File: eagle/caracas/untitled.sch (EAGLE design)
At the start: 26 parts, among them IC1 4027N, Q1 IRFP250, X1 22-23-2021, X2 22-23-2021, X3 22-23-2041, X4 22-23-2041, X5 22-23-2021, X6 22-23-2021

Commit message: Schematic and board finished (at least R1)
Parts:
- Q1: value IRFP250 -> IRLZ44Z; device transistor-power:IRFP250 -> transistor-power:IRLZ44Z
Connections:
- net +12V_IGN: now also U$2G$4.P$1; no longer U$2G$3.P$1
- net +3.3V: now also X4-1.S, X4-2.S; no longer X3-1.S, X4-4.S
- net ANA_1: now also X4-4.S; no longer X4-2.S
- net GND: no longer X4-1.S
- net VCC: now also U$2G$3.P$1; no longer U$2G$2.P$1
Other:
- moved on the sheet: X3-1, X4-1, X4-2, X4-4
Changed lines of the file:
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@@
 <grid distance="0.1" unitdist="inch" unit="inch" style="lines" multiple="1" display="no" altdistance="0.01" altunitdist="inch" altunit="inch"/>
 <layers>
-<layer number="1" name="Top" color="4" fill="1" visible="no" active="no"/>
-<layer number="16" name="Bottom" color="1" fill="1" visible="no" active="no"/>
-<layer number="17" name="Pads" color="2" fill="1" visible="no" active="no"/>
-<layer number="18" name="Vias" color="2" fill="1" visible="no" active="no"/>
-<layer number="19" name="Unrouted" color="6" fill="1" visible="no" active="no"/>
-<layer number="20" name="Dimension" color="15" fill="1" visible="no" active="no"/>
-<layer number="21" name="tPlace" color="7" fill="1" visible="no" active="no"/>
-<layer number="22" name="bPlace" color="7" fill="1" visible="no" active="no"/>
-<layer number="23" name="tOrigins" color="15" fill="1" visible="no" active="no"/>
-<layer number="24" name="bOrigins" color="15" fill="1" visible="no" active="no"/>
-<layer number="25" name="tNames" color="7" fill="1" visible="no" active="no"/>
-<layer number="26" name="bNames" color="7" fill="1" visible="no" active="no"/>
-<layer number="27" name="tValues" color="7" fill="1" visible="no" active="no"/>
-<layer number="28" name="bValues" color="7" fill="1" visible="no" active="no"/>
+<layer number="1" name="Top" color="4" fill="1" visible="yes" active="no"/>
+<layer number="16" name="Bottom" color="1" fill="1" visible="yes" active="no"/>
+<layer number="17" name="Pads" color="2" fill="1" visible="yes" active="no"/>
+<layer number="18" name="Vias" color="2" fill="1" visible="yes" active="no"/>
+<layer number="19" name="Unrouted" color="6" fill="1" visible="yes" active="no"/>
+<layer number="20" name="Dimension" color="15" fill="1" visible="yes" active="no"/>
+<layer number="21" name="tPlace" color="7" fill="1" visible="yes" active="no"/>
+<layer number="22" name="bPlace" color="7" fill="1" visible="yes" active="no"/>
+<layer number="23" name="tOrigins" color="15" fill="1" visible="yes" active="no"/>
+<layer number="24" name="bOrigins" color="15" fill="1" visible="yes" active="no"/>
+<layer number="25" name="tNames" color="7" fill="1" visible="yes" active="no"/>
+<layer number="26" name="bNames" color="7" fill="1" visible="yes" active="no"/>
+<layer number="27" name="tValues" color="7" fill="1" visible="yes" active="no"/>
+<layer number="28" name="bValues" color="7" fill="1" visible="yes" active="no"/>
 <layer number="29" name="tStop" color="7" fill="3" visible="no" active="no"/>
 <layer number="30" name="bStop" color="7" fill="6" visible="no" active="no"/>
@@
 <layer number="35" name="tGlue" color="7" fill="4" visible="no" active="no"/>
 <layer number="36" name="bGlue" color="7" fill="5" visible="no" active="no"/>
-<layer number="37" name="tTest" color="7" fill="1" visible="no" active="no"/>
-<layer number="38" name="bTest" color="7" fill="1" visible="no" active="no"/>
+<layer number="37" name="tTest" color="7" fill="1" visible="yes" active="no"/>
+<layer number="38" name="bTest" color="7" fill="1" visible="yes" active="no"/>
 <layer number="39" name="tKeepout" color="4" fill="11" visible="no" active="no"/>
 <layer number="40" name="bKeepout" color="1" fill="11" visible="no" active="no"/>
@@
 <layer number="44" name="Drills" color="7" fill="1" visible="no" active="no"/>
 <layer number="45" name="Holes" color="7" fill="1" visible="no" active="no"/>
-<layer number="46" name="Milling" color="3" fill="1" visible="no" active="no"/>
-<layer number="47" name="Measures" color="7" fill="1" visible="no" active="no"/>
-<layer number="48" name="Document" color="7" fill="1" visible="no" active="no"/>
-<layer number="49" name="Reference" color="7" fill="1" visible="no" active="no"/>
-<layer number="51" name="tDocu" color="7" fill="1" visible="no" active="no"/>
-<layer number="52" name="bDocu" color="7" fill="1" visible="no" active="no"/>
+<layer number="46" name="Milling" color="3" fill="1" visible="yes" active="no"/>
+<layer number="47" name="Measures" color="7" fill="1" visible="yes" active="no"/>
+<layer number="48" name="Document" color="7" fill="1" visible="yes" active="no"/>
+<layer number="49" name="Reference" color="7" fill="1" visible="yes" active="no"/>
+<layer number="51" name="tDocu" color="7" fill="1" visible="yes" active="no"/>
+<layer number="52" name="bDocu" color="7" fill="1" visible="yes" active="no"/>
 <layer number="91" name="Nets" color="2" fill="1" visible="yes" active="yes"/>
 <layer number="92" name="Busses" color="1" fill="1" visible="yes" active="yes"/>
@@
 <part name="R5" library="rcl" deviceset="R-EU_" device="0207/10"/>
 <part name="R3" library="rcl" deviceset="R-EU_" device="0207/10"/>
-<part name="Q1" library="transistor-power" deviceset="IRFP25*" device="" technology="0"/>
 <part name="SUPPLY3" library="supply2" deviceset="GND" device=""/>
 <part name="R8" library="rcl" deviceset="R-EU_" device="0207/10"/>
@@
 <part name="X3" library="con-molex" deviceset="22-23-2041" device=""/>
 <part name="X4" library="con-molex" deviceset="22-23-2041" device=""/>
+<part name="Q1" library="transistor-power" deviceset="IRLZ44Z" device=""/>
 </parts>
 <sheets>
@@
 <instance part="R5" gate="G$1" x="43.18" y="38.1" rot="R270"/>
 <instance part="R3" gate="G$1" x="99.06" y="45.72"/>
-<instance part="Q1" gate="G$1" x="114.3" y="48.26"/>
 <instance part="SUPPLY3" gate="GND" x="-48.26" y="2.54"/>
 <instance part="R8" gate="G$1" x="-76.2" y="-12.7" rot="R90"/>
@@
 <instance part="R11" gate="G$1" x="88.9" y="-43.18" rot="R90"/>
 <instance part="R12" gate="G$1" x="93.98" y="-43.18" rot="R90"/>
-<instance part="X3" gate="-1" x="-63.5" y="-38.1" rot="R270"/>
+<instance part="X4" gate="-1" x="-63.5" y="-38.1" rot="R270"/>
 <instance part="X3" gate="-2" x="-66.04" y="-38.1" rot="R270"/>
 <instance part="X3" gate="-3" x="-68.58" y="-38.1" rot="R270"/>
 <instance part="X3" gate="-4" x="-71.12" y="-38.1" rot="R270"/>
-<instance part="X4" gate="-1" x="-53.34" y="-38.1" rot="R270"/>
-<instance part="X4" gate="-2" x="-55.88" y="-38.1" rot="R270"/>
+<instance part="X3" gate="-1" x="-53.34" y="-38.1" rot="R270"/>
+<instance part="X4" gate="-4" x="-55.88" y="-38.1" rot="R270"/>
 <instance part="X4" gate="-3" x="-58.42" y="-38.1" rot="R270"/>
-<instance part="X4" gate="-4" x="-60.96" y="-38.1" rot="R270"/>
-<instance part="U$2" gate="G$2" x="-2.54" y="-60.96" rot="R270"/>
-<instance part="U$2" gate="G$3" x="2.54" y="-60.96" rot="R270"/>
+<instance part="X4" gate="-2" x="-60.96" y="-38.1" rot="R270"/>
+<instance part="U$2" gate="G$3" x="-2.54" y="-60.96" rot="R270"/>
+<instance part="U$2" gate="G$4" x="2.54" y="-60.96" rot="R270"/>
+<instance part="Q1" gate="G$1" x="114.3" y="48.26"/>
 </instances>
 <busses>
@@
 <wire x1="53.34" y1="17.78" x2="91.44" y2="17.78" width="0.1524" layer="91"/>
 <junction x="91.44" y="17.78"/>
-<pinref part="Q1" gate="G$1" pin="S"/>
 <wire x1="91.44" y1="17.78" x2="116.84" y2="17.78" width="0.1524" layer="91"/>
 <wire x1="116.84" y1="17.78" x2="116.84" y2="43.18" width="0.1524" layer="91"/>
@@
 <pinref part="R6" gate="G$1" pin="1"/>
 <wire x1="53.34" y1="17.78" x2="53.34" y2="22.86" width="0.1524" layer="91"/>
+<pinref part="Q1" gate="G$1" pin="S"/>
 </segment>
 <segment>
@@
 <junction x="-48.26" y="10.16"/>
 <pinref part="SUPPLY3" gate="GND" pin="GND"/>
-<wire x1="-53.34" y1="-35.56" x2="-53.34" y2="10.16" width="0.1524" layer="91"/>
 <wire x1="-53.34" y1="10.16" x2="-48.26" y2="10.16" width="0.1524" layer="91"/>
-<pinref part="X4" gate="-1" pin="S"/>
+<wire x1="-53.34" y1="10.16" x2="-53.34" y2="-30.48" width="0.1524" layer="91"/>
 </segment>
 <segment>
@@
 <label x="2.54" y="-25.4" size="1.778" layer="95"/>
 <wire x1="2.54" y1="-27.94" x2="2.54" y2="-55.88" width="0.1524" layer="91"/>
-<pinref part="U$2" gate="G$3" pin="P$1"/>
+<pinref part="U$2" gate="G$4" pin="P$1"/>
 </segment>
 <segment>
@@
 <wire x1="-63.5" y1="-25.4" x2="-63.5" y2="-35.56" width="0.1524" layer="91"/>
 <junction x="-63.5" y="-25.4"/>
-<pinref part="X3" gate="-1" pin="S"/>
-<pinref part="X4" gate="-4" pin="S"/>
+<pinref part="X4" gate="-1" pin="S"/>
+<pinref part="X4" gate="-2" pin="S"/>
 </segment>
 </net>
@@
 <wire x1="-71.12" y1="-20.32" x2="-55.88" y2="-20.32" width="0.1524" layer="91"/>
 <junction x="-55.88" y="-20.32"/>
-<pinref part="X4" gate="-2" pin="S"/>
+<pinref part="X4" gate="-4" pin="S"/>
 </segment>
 </net>
@@
 <wire x1="-7.62" y1="-35.56" x2="-2.54" y2="-35.56" width="0.1524" layer="91"/>
 <junction x="-2.54" y="-33.02"/>
-<pinref part="U$2" gate="G$2" pin="P$1"/>
 <wire x1="-2.54" y1="-35.56" x2="-2.54" y2="-55.88" width="0.1524" layer="91"/>
 <junction x="-2.54" y="-35.56"/>
-</segment>
-</net>
+<pinref part="U$2" gate="G$3" pin="P$1"/>
+</segment>
+</net>

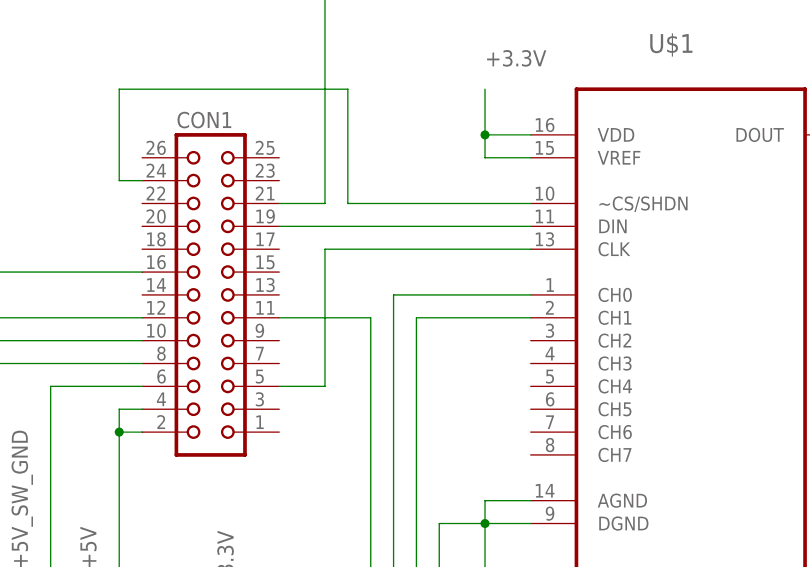
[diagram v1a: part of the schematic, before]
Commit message: SPI clock in on pin 23, not pin 5
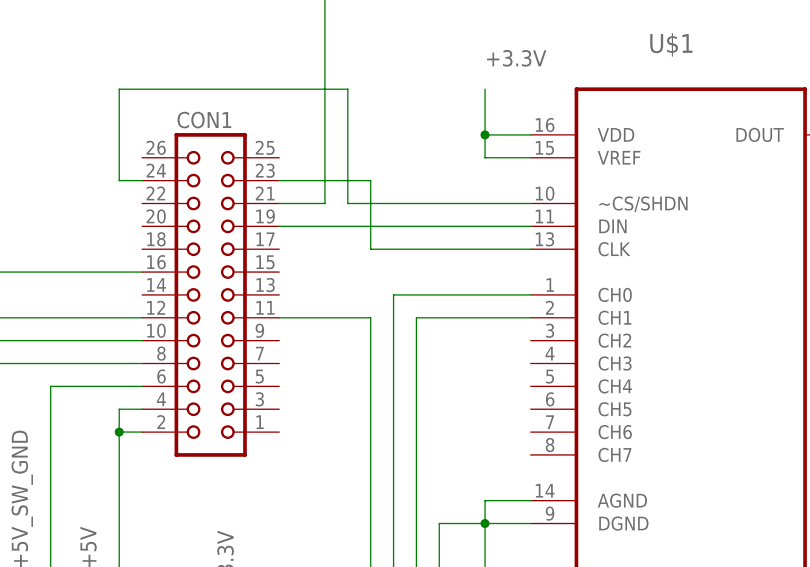
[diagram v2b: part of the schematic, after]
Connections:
- net N$3: now also CON1.23; no longer CON1.5
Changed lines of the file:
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@@
 <grid distance="0.1" unitdist="inch" unit="inch" style="lines" multiple="1" display="no" altdistance="0.01" altunitdist="inch" altunit="inch"/>
 <layers>
-<layer number="1" name="Top" color="4" fill="1" visible="yes" active="no"/>
-<layer number="16" name="Bottom" color="1" fill="1" visible="yes" active="no"/>
-<layer number="17" name="Pads" color="2" fill="1" visible="yes" active="no"/>
-<layer number="18" name="Vias" color="2" fill="1" visible="yes" active="no"/>
-<layer number="19" name="Unrouted" color="6" fill="1" visible="yes" active="no"/>
-<layer number="20" name="Dimension" color="15" fill="1" visible="yes" active="no"/>
-<layer number="21" name="tPlace" color="7" fill="1" visible="yes" active="no"/>
-<layer number="22" name="bPlace" color="7" fill="1" visible="yes" active="no"/>
-<layer number="23" name="tOrigins" color="15" fill="1" visible="yes" active="no"/>
-<layer number="24" name="bOrigins" color="15" fill="1" visible="yes" active="no"/>
-<layer number="25" name="tNames" color="7" fill="1" visible="yes" active="no"/>
-<layer number="26" name="bNames" color="7" fill="1" visible="yes" active="no"/>
-<layer number="27" name="tValues" color="7" fill="1" visible="yes" active="no"/>
-<layer number="28" name="bValues" color="7" fill="1" visible="yes" active="no"/>
+<layer number="1" name="Top" color="4" fill="1" visible="no" active="no"/>
+<layer number="16" name="Bottom" color="1" fill="1" visible="no" active="no"/>
+<layer number="17" name="Pads" color="2" fill="1" visible="no" active="no"/>
+<layer number="18" name="Vias" color="2" fill="1" visible="no" active="no"/>
+<layer number="19" name="Unrouted" color="6" fill="1" visible="no" active="no"/>
+<layer number="20" name="Dimension" color="15" fill="1" visible="no" active="no"/>
+<layer number="21" name="tPlace" color="7" fill="1" visible="no" active="no"/>
+<layer number="22" name="bPlace" color="7" fill="1" visible="no" active="no"/>
+<layer number="23" name="tOrigins" color="15" fill="1" visible="no" active="no"/>
+<layer number="24" name="bOrigins" color="15" fill="1" visible="no" active="no"/>
+<layer number="25" name="tNames" color="7" fill="1" visible="no" active="no"/>
+<layer number="26" name="bNames" color="7" fill="1" visible="no" active="no"/>
+<layer number="27" name="tValues" color="7" fill="1" visible="no" active="no"/>
+<layer number="28" name="bValues" color="7" fill="1" visible="no" active="no"/>
 <layer number="29" name="tStop" color="7" fill="3" visible="no" active="no"/>
 <layer number="30" name="bStop" color="7" fill="6" visible="no" active="no"/>
@@
 <layer number="35" name="tGlue" color="7" fill="4" visible="no" active="no"/>
 <layer number="36" name="bGlue" color="7" fill="5" visible="no" active="no"/>
-<layer number="37" name="tTest" color="7" fill="1" visible="yes" active="no"/>
-<layer number="38" name="bTest" color="7" fill="1" visible="yes" active="no"/>
+<layer number="37" name="tTest" color="7" fill="1" visible="no" active="no"/>
+<layer number="38" name="bTest" color="7" fill="1" visible="no" active="no"/>
 <layer number="39" name="tKeepout" color="4" fill="11" visible="no" active="no"/>
 <layer number="40" name="bKeepout" color="1" fill="11" visible="no" active="no"/>
@@
 <layer number="44" name="Drills" color="7" fill="1" visible="no" active="no"/>
 <layer number="45" name="Holes" color="7" fill="1" visible="no" active="no"/>
-<layer number="46" name="Milling" color="3" fill="1" visible="yes" active="no"/>
-<layer number="47" name="Measures" color="7" fill="1" visible="yes" active="no"/>
-<layer number="48" name="Document" color="7" fill="1" visible="yes" active="no"/>
-<layer number="49" name="Reference" color="7" fill="1" visible="yes" active="no"/>
-<layer number="51" name="tDocu" color="7" fill="1" visible="yes" active="no"/>
-<layer number="52" name="bDocu" color="7" fill="1" visible="yes" active="no"/>
+<layer number="46" name="Milling" color="3" fill="1" visible="no" active="no"/>
+<layer number="47" name="Measures" color="7" fill="1" visible="no" active="no"/>
+<layer number="48" name="Document" color="7" fill="1" visible="no" active="no"/>
+<layer number="49" name="Reference" color="7" fill="1" visible="no" active="no"/>
+<layer number="51" name="tDocu" color="7" fill="1" visible="no" active="no"/>
+<layer number="52" name="bDocu" color="7" fill="1" visible="no" active="no"/>
 <layer number="91" name="Nets" color="2" fill="1" visible="yes" active="yes"/>
 <layer number="92" name="Busses" color="1" fill="1" visible="yes" active="yes"/>
@@
 </segment>
 </net>
-<net name="N$3" class="0">
-<segment>
-<pinref part="CON1" gate="A" pin="5"/>
-<wire x1="-71.12" y1="25.4" x2="-66.04" y2="25.4" width="0.1524" layer="91"/>
-<wire x1="-66.04" y1="25.4" x2="-66.04" y2="40.64" width="0.1524" layer="91"/>
-<pinref part="U$1" gate="A" pin="CLK"/>
-<wire x1="-66.04" y1="40.64" x2="-43.18" y2="40.64" width="0.1524" layer="91"/>
-</segment>
-</net>
 <net name="N$4" class="0">
 <segment>
@@
 </segment>
 </net>
+<net name="N$3" class="0">
+<segment>
+<pinref part="U$1" gate="A" pin="CLK"/>
+<wire x1="-43.18" y1="40.64" x2="-60.96" y2="40.64" width="0.1524" layer="91"/>
+<wire x1="-60.96" y1="40.64" x2="-60.96" y2="48.26" width="0.1524" layer="91"/>
+<pinref part="CON1" gate="A" pin="23"/>
+<wire x1="-60.96" y1="48.26" x2="-71.12" y2="48.26" width="0.1524" layer="91"/>
+</segment>
+</net>

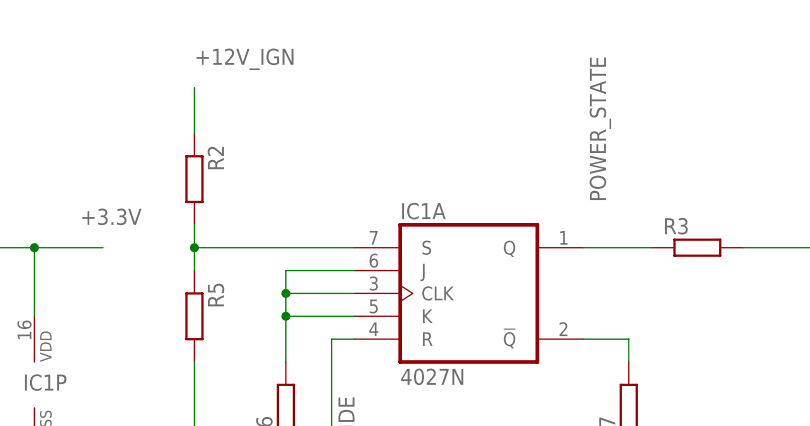
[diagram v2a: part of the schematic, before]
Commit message: Fixed errors in the electrical diagram.
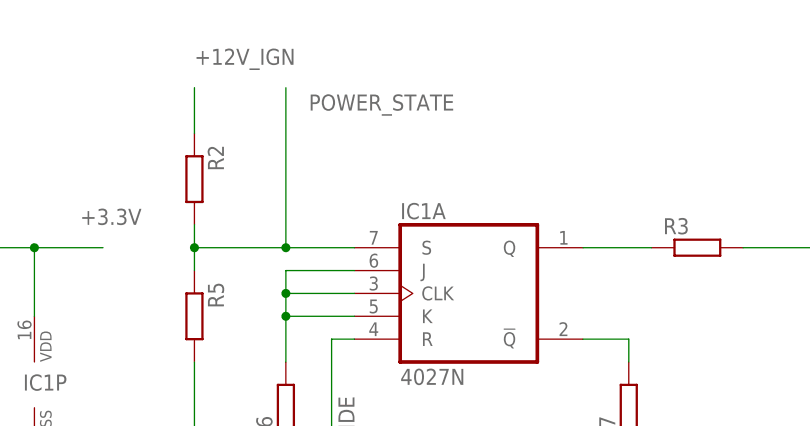
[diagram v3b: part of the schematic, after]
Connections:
- removed net +3.3V1: IC1A.S, R2.2, R5.1
- new net N$14: IC1A.Q, R3.1
- net POWER_STATE: now also IC1A.S, R2.2, R5.1; no longer IC1A.Q, R3.1
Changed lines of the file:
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@@
 <net name="POWER_STATE" class="0">
-<segment>
-<pinref part="IC1" gate="A" pin="Q"/>
-<wire x1="86.36" y1="45.72" x2="93.98" y2="45.72" width="0.1524" layer="91"/>
-<pinref part="R3" gate="G$1" pin="1"/>
-<label x="88.9" y="50.8" size="1.778" layer="95" rot="R90"/>
-</segment>
 <segment>
 <wire x1="-86.36" y1="38.1" x2="-116.84" y2="38.1" width="0.1524" layer="91"/>
 <label x="-119.38" y="38.1" size="1.778" layer="95" rot="R90"/>
 <pinref part="CON1" gate="A" pin="16"/>
+</segment>
+<segment>
+<wire x1="43.18" y1="48.26" x2="43.18" y2="45.72" width="0.1524" layer="91"/>
+<wire x1="43.18" y1="45.72" x2="43.18" y2="43.18" width="0.1524" layer="91"/>
+<wire x1="43.18" y1="45.72" x2="53.34" y2="45.72" width="0.1524" layer="91"/>
+<junction x="43.18" y="45.72"/>
+<pinref part="IC1" gate="A" pin="S"/>
+<pinref part="R2" gate="G$1" pin="2"/>
+<pinref part="R5" gate="G$1" pin="1"/>
+<wire x1="53.34" y1="45.72" x2="60.96" y2="45.72" width="0.1524" layer="91"/>
+<wire x1="53.34" y1="45.72" x2="53.34" y2="63.5" width="0.1524" layer="91"/>
+<junction x="53.34" y="45.72"/>
+<label x="55.88" y="60.96" size="1.778" layer="95"/>
 </segment>
 </net>
@@
 <pinref part="X4" gate="-1" pin="S"/>
 <pinref part="X4" gate="-2" pin="S"/>
-</segment>
-</net>
-<net name="+3.3V1" class="0">
-<segment>
-<wire x1="43.18" y1="48.26" x2="43.18" y2="45.72" width="0.1524" layer="91"/>
-<wire x1="43.18" y1="45.72" x2="43.18" y2="43.18" width="0.1524" layer="91"/>
-<wire x1="43.18" y1="45.72" x2="60.96" y2="45.72" width="0.1524" layer="91"/>
-<junction x="43.18" y="45.72"/>
-<pinref part="IC1" gate="A" pin="S"/>
-<pinref part="R2" gate="G$1" pin="2"/>
-<pinref part="R5" gate="G$1" pin="1"/>
 </segment>
 </net>
@@
 </segment>
 </net>
+<net name="N$14" class="0">
+<segment>
+<pinref part="IC1" gate="A" pin="Q"/>
+<pinref part="R3" gate="G$1" pin="1"/>
+<wire x1="86.36" y1="45.72" x2="93.98" y2="45.72" width="0.1524" layer="91"/>
+</segment>
+</net>

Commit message: Schematics: replace CD4027N J/K flip-flop with 4011N nand gates.
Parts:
- removed IC1: 4027N, 40xx:4027N
- removed R1, R10, R11, R12, R3, R4, R6, R7: (no value), rcl:R-EU_0207/10
- added D1: 1N4728, diode:1N4728
- added IC2: 4011N, 40xx:4011N
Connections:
- removed net N$11: IC1B.!Q, R11.2
- removed net N$12: IC1B.CLK, IC1B.J, IC1B.K, IC1B.R, IC1B.S, R10.2
- removed net N$13: IC1B.Q, R12.2
- removed net N$14: IC1A.Q, R3.1
- removed net N$2: IC1A.!Q, R7.2
- removed net N$9: IC1A.CLK, IC1A.J, IC1A.K, R6.2
- removed net SUICIDE: CON1.11, IC1A.R
- new net N$16: IC2A.I1, IC2B.O
- new net RPI_RESET: CON1.11, IC2B.I1
- new net RPI_SET: IC2A.I0
- net +3.3V: now also CON1.1; no longer IC1P.VDD, R1.2, R4.1
- net +5V: now also IC2P.VDD; no longer R1.1
- net GND: now also D1.A, IC2P.VSS; no longer IC1P.VSS, R10.1, R11.1, R12.1, R4.2, R6.1, R7.1
- net N$1: now also IC2A.O, IC2B.I0; no longer R3.2
- net POWER_STATE: now also D1.C; no longer IC1A.S
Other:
- moved on the sheet: Q1, R2, R5
